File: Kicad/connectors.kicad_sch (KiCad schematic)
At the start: 22 parts, among them J1 HM_10_BLE_Module, J10 VL53L0CXV0DH - TOF, J11 DFPlayer_Left, J12 Speaker, J13 DFPlayer_Right, J3 APDS9960, J4 Neopixel, J5 Motor_Left, J6 Motor_Right, J7 MPU-6050, J8 Servo_Left, J9 Servo_Right

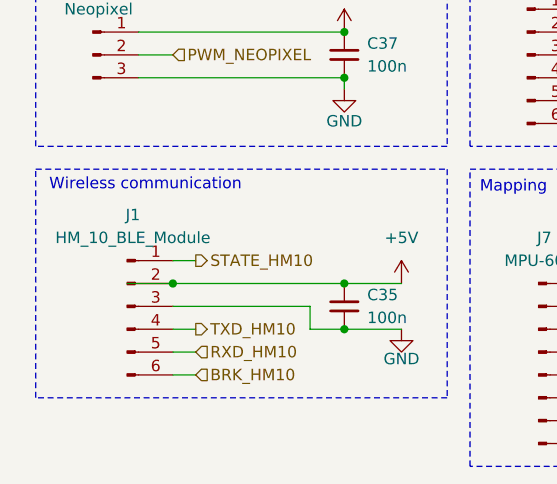
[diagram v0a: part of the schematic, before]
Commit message: chore: redid placement from the ground up
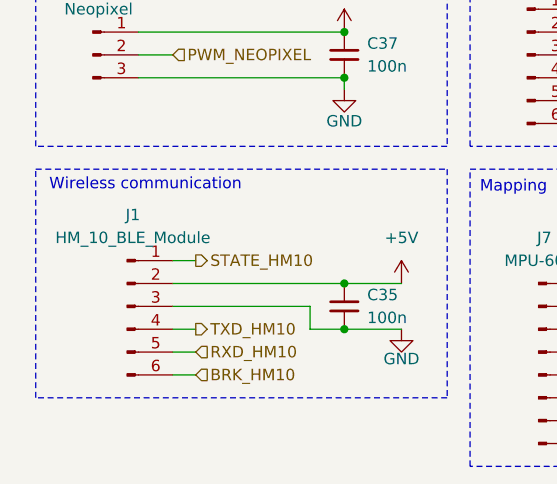
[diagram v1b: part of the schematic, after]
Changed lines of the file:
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@@
-	)
-	(junction
-		(at 34.29 81.28)
-		(diameter 0)
-		(color 0 0 0 0)
 	)
 	(junction
@@
 		)
 		(stroke
-			(width 0)
-			(type default)
-		)
-	)
-	(wire
-		(pts
-			(xy 29.21 81.28) (xy 34.29 81.28)
-		)
-		(stroke
